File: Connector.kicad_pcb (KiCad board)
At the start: 2 copper layers, 77 x 16.1 mm, 1 part, among them J1 776163-1

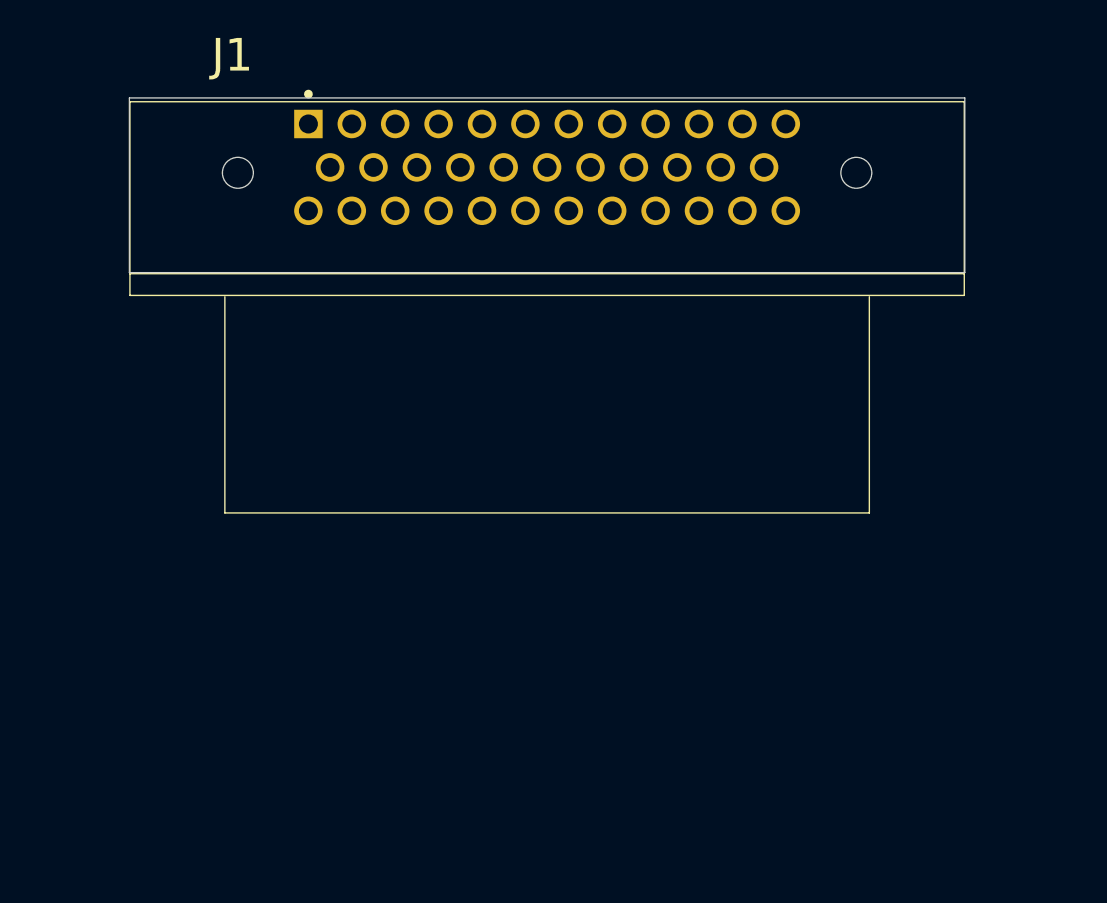
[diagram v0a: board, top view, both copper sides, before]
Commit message: Added PCB Outline
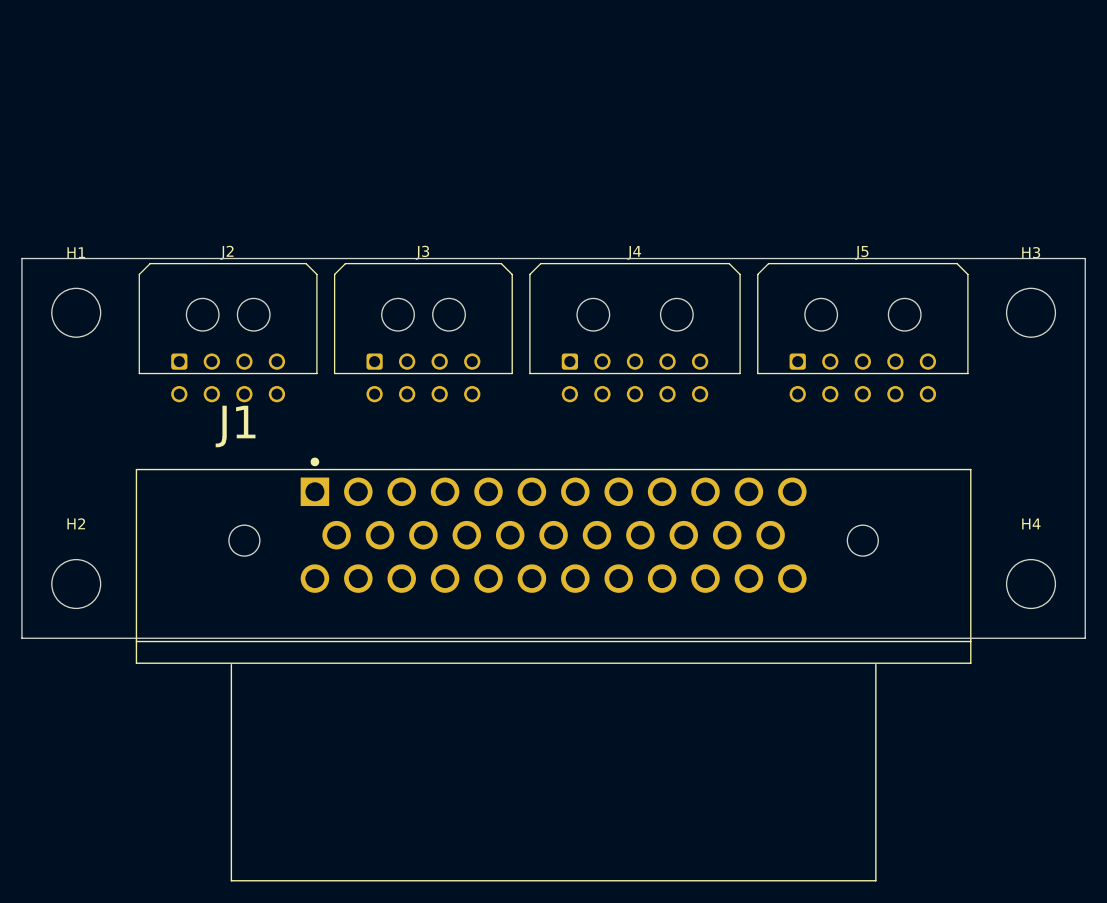
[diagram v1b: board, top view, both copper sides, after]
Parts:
- added H1: MountingHole, MountingHole:MountingHole_4.5mm, F.Cu at (85.5, 105.0)
- added H2: MountingHole, MountingHole:MountingHole_4.5mm, F.Cu at (85.5, 130.0)
- added H3: MountingHole, MountingHole:MountingHole_4.5mm, F.Cu at (173.5, 105.0)
- added H4: MountingHole, MountingHole:MountingHole_4.5mm, F.Cu at (173.5, 130.0)
- added J2: Conn_02x04_Odd_Even, MyLibrary:Molex_Micro-Fit_3.0_43045-0800_2x04_P3.00mm_Horizontal, F.Cu at (95.0, 109.5)
- added J3: Conn_02x04_Odd_Even, MyLibrary:Molex_Micro-Fit_3.0_43045-0800_2x04_P3.00mm_Horizontal, F.Cu at (113.0, 109.5)
- added J4: Conn_02x05_Odd_Even, MyLibrary:Molex_Micro-Fit_3.0_43045-1000_2x05_P3.00mm_Horizontal, F.Cu at (131.0, 109.5)
- added J5: Conn_02x05_Odd_Even, MyLibrary:Molex_Micro-Fit_3.0_43045-1000_2x05_P3.00mm_Horizontal, F.Cu at (152.0, 109.5)
- moved J1 33.9 mm to (129.5, 126.0)
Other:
- board size 77 x 16.1 mm -> 98 x 35 mm

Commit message: Added Connector PinOut and PCB layout
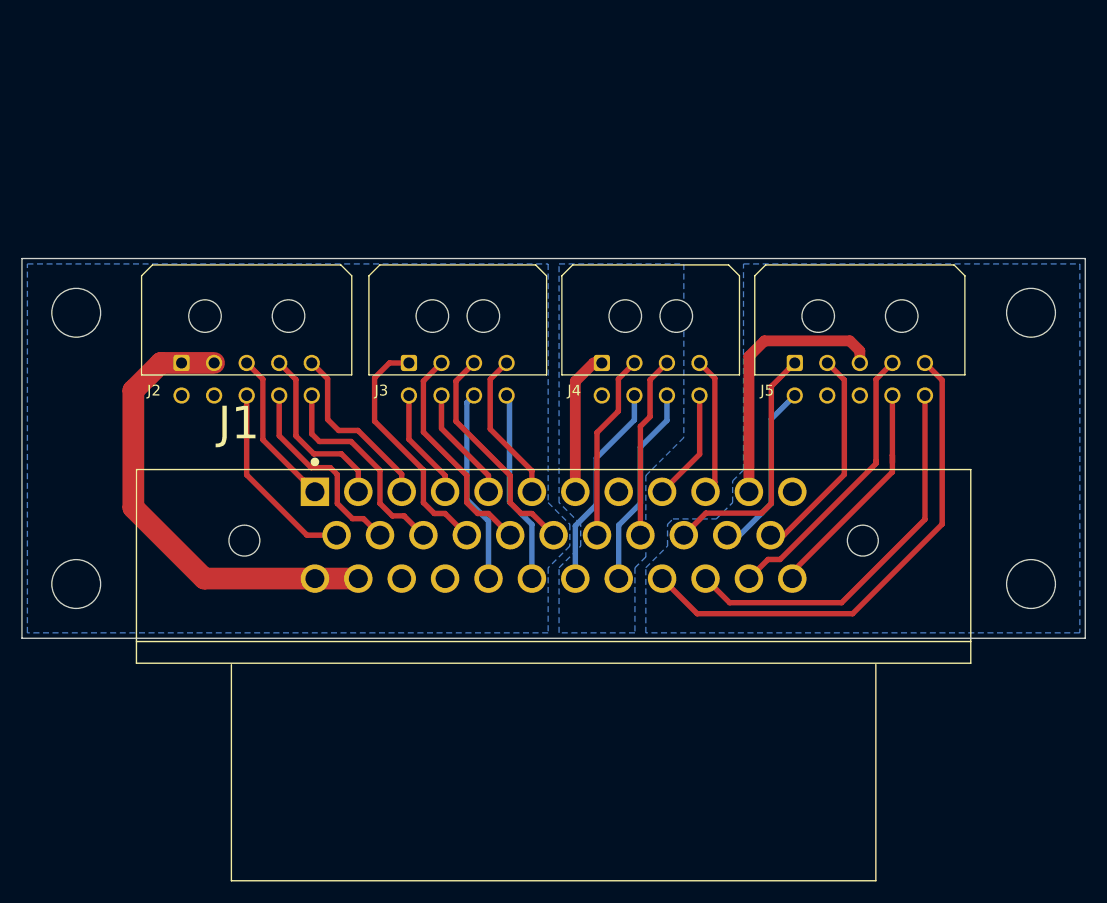
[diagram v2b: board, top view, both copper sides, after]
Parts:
- J2: value Conn_02x04_Odd_Even -> Conn_02x05_Top_Bottom; footprint MyLibrary:Molex_Micro-Fit_3.0_43045-0800_2x04_P3.00mm_Horizontal -> MyLibrary:Molex_Micro-Fit_3.0_43045-1000_2x05_P3.00mm_Horizontal
- J3: value Conn_02x04_Odd_Even -> Conn_02x04_Top_Bottom
- J4: value Conn_02x05_Odd_Even -> Conn_02x04_Top_Bottom; footprint MyLibrary:Molex_Micro-Fit_3.0_43045-1000_2x05_P3.00mm_Horizontal -> MyLibrary:Molex_Micro-Fit_3.0_43045-0800_2x04_P3.00mm_Horizontal
- J5: value Conn_02x05_Odd_Even -> Conn_02x05_Top_Bottom
- moved J3 3.17 mm to (116.2, 109.6)
- moved J4 2.95 mm to (133.9, 109.6)
- moved J5 0.30 mm to (151.7, 109.6)
- moved J2 0.24 mm to (95.2, 109.6)
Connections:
- J1 pad 1: Net-(J1-Pad1) -> /PowerSteeringPWM
- J1 pad 10: Net-(J1-Pad10) -> /CAN_L
- J1 pad 11: Net-(J1-Pad11) -> +5VD
- J1 pad 12: Net-(J1-Pad12) -> GNDD
- J1 pad 13: Net-(J1-Pad13) -> /ShuntContactorOn
- J1 pad 14: Net-(J1-Pad14) -> /ReverseLight
- J1 pad 15: Net-(J1-Pad15) -> /Pump
- J1 pad 16: Net-(J1-Pad16) -> /GearDrive
- J1 pad 17: Net-(J1-Pad17) -> /GearReverse
- J1 pad 18: Net-(J1-Pad18) -> /GearParking
- J1 pad 19: Net-(J1-Pad19) -> /Brake_2
- J1 pad 2: Net-(J1-Pad2) -> /ParkingBrake
- J1 pad 20: Net-(J1-Pad20) -> /Brake_1
- J1 pad 21: Net-(J1-Pad21) -> /HALL_3
- J1 pad 22: Net-(J1-Pad22) -> /HALL_2
- J1 pad 23: Net-(J1-Pad23) -> /HALL_1
- J1 pad 24: Net-(J1-Pad24) -> VDD
- J1 pad 25: Net-(J1-Pad25) -> VDD
- J1 pad 26: Net-(J1-Pad26) -> GND
- J1 pad 27: Net-(J1-Pad27) -> GND
- J1 pad 28: Net-(J1-Pad28) -> /RightSupport
- J1 pad 29: Net-(J1-Pad29) -> /LeftSupport
- J1 pad 3: Net-(J1-Pad3) -> /PowerContactorOn
- J1 pad 30: Net-(J1-Pad30) -> /Accelerator_2
- J1 pad 31: Net-(J1-Pad31) -> /Accelerator_1
- J1 pad 32: Net-(J1-Pad32) -> /NTC_AW_2
- J1 pad 33: Net-(J1-Pad33) -> /NTC_AW_1
- J1 pad 34: Net-(J1-Pad34) -> /NTC_FW_2
- J1 pad 35: Net-(J1-Pad35) -> /NTC_FW_1
- J1 pad 4: Net-(J1-Pad4) -> /HighVoltageOn
- J1 pad 5: Net-(J1-Pad5) -> /IgnitionOn
- J1 pad 6: Net-(J1-Pad6) -> /EmergencyStop
- J1 pad 7: Net-(J1-Pad7) -> +5VA
- J1 pad 8: Net-(J1-Pad8) -> GNDA
- J1 pad 9: Net-(J1-Pad9) -> /CAN_H
- J2 pad 2: GND -> VDD
- J2 pad 3: /ParkingBrake -> /PowerSteeringPWM
- J2 pad 4: /ReverseLight -> /ParkingBrake
- J2 pad 5: /ShuntContactorOn -> /PowerContactorOn
- J2 pad 6: /PowerContactorOn -> GND
- J2 pad 7: /Pump -> GND
- J2 pad 8: /PowerSteeringPWM -> /ShuntContactorOn
- J3 pad 1: /LeftSupport -> /GearDrive
- J3 pad 2: /RightSupport -> /GearReverse
- J3 pad 3: /HighVoltageOn -> /GearParking
- J3 pad 4: /IgnitionOn -> /EmergencyStop
- J3 pad 5: /GearReverse -> /HighVoltageOn
- J3 pad 6: /GearDrive -> /IgnitionOn
- J3 pad 7: /EmergencyStop -> /RightSupport
- J3 pad 8: /GearParking -> /LeftSupport
- J4 pad 2: GNDA -> /Brake_2
- J4 pad 3: /Accelerator_1 -> /Brake_1
- J4 pad 4: /Accelerator_2 -> /CAN_L
- J4 pad 5: +5VA -> GNDA
- J4 pad 6: GNDA -> /Accelerator_2
- J4 pad 7: /Brake_1 -> /Accelerator_1
- J4 pad 8: /Brake_2 -> /CAN_H
- J5 pad 1: /HALL_1 -> /HALL_3
- J5 pad 2: /HALL_2 -> /HALL_1
- J5 pad 3: /HALL_3 -> +5VD
- J5 pad 4: Net-(J5-Pad4) -> /NTC_FW_2
- J5 pad 5: +5VD -> /NTC_AW_2
- J5 pad 6: GNDD -> /HALL_2
- J5 pad 7: /NTC_FW_2 -> GNDD
- J5 pad 8: /NTC_FW_1 -> GNDD
- J5 pad 9: /NTC_AW_2 -> /NTC_FW_1
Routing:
- net /NTC_AW_2: track 0.00 -> 46.1 mm
- net VDD: track 0.00 -> 42.7 mm
- net /NTC_AW_1: track 0.00 -> 35.7 mm
- net /NTC_FW_2: track 0.00 -> 26.0 mm
- net +5VD: track 0.00 -> 24.8 mm
- net /HALL_3: track 0.00 -> 23.1 mm
- net /GearDrive: track 0.00 -> 22.3 mm
- net /NTC_FW_1: track 0.00 -> 21.5 mm
- net /GearParking: track 0.00 -> 20.9 mm
- net /GearReverse: track 0.00 -> 20.5 mm
- net /HALL_1: track 0.00 -> 20.0 mm
- net /Pump: track 0.00 -> 19.5 mm
- net /Accelerator_2: track 0.00 -> 19.1 mm
- net /Accelerator_1: track 0.00 -> 18.7 mm
- net /ReverseLight: track 0.00 -> 18.4 mm
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- added copper zone on B.Cu, net GND
- added copper zone on B.Cu, net GNDA
- added copper zone on B.Cu, net GNDD

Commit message: Added Gerbers
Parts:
- added G***: LOGO, MyLibrary:Ecio_Logo, B.Cu at (172.0, 117.0)
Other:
- board text added: "J1"
- board text added: "J2"
- board text added: "J3"
- board text added: "J4"
- board text added: "J5"
- board text added: "Rev A"
